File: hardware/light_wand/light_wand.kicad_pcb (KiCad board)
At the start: 2 copper layers, 21 parts, among them J1 1x1 Conn, J2 1x1 Conn, J3 1x1 Conn, J4 1x1 Conn, J5 1x1 Conn, J6 1x1 Conn, U1 TLV61070A, U4 Pico

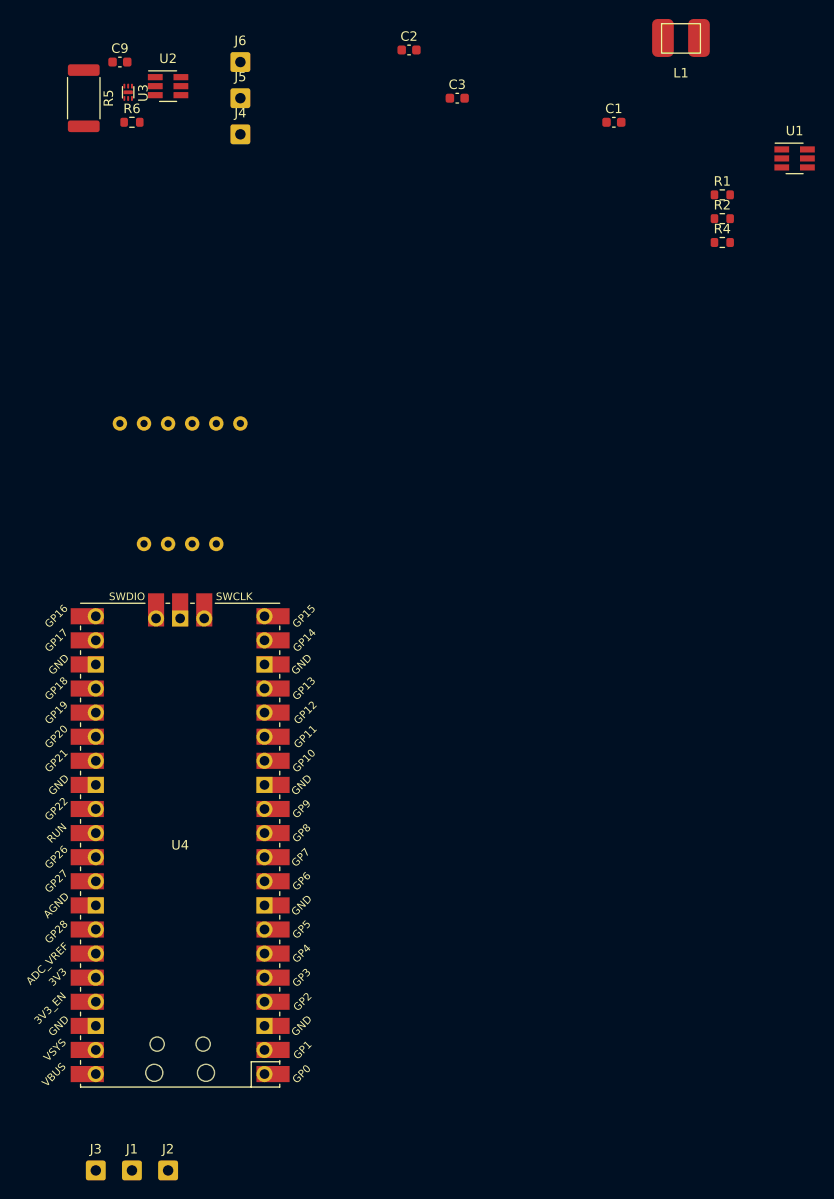
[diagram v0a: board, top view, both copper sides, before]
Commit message: Finished PCB layout
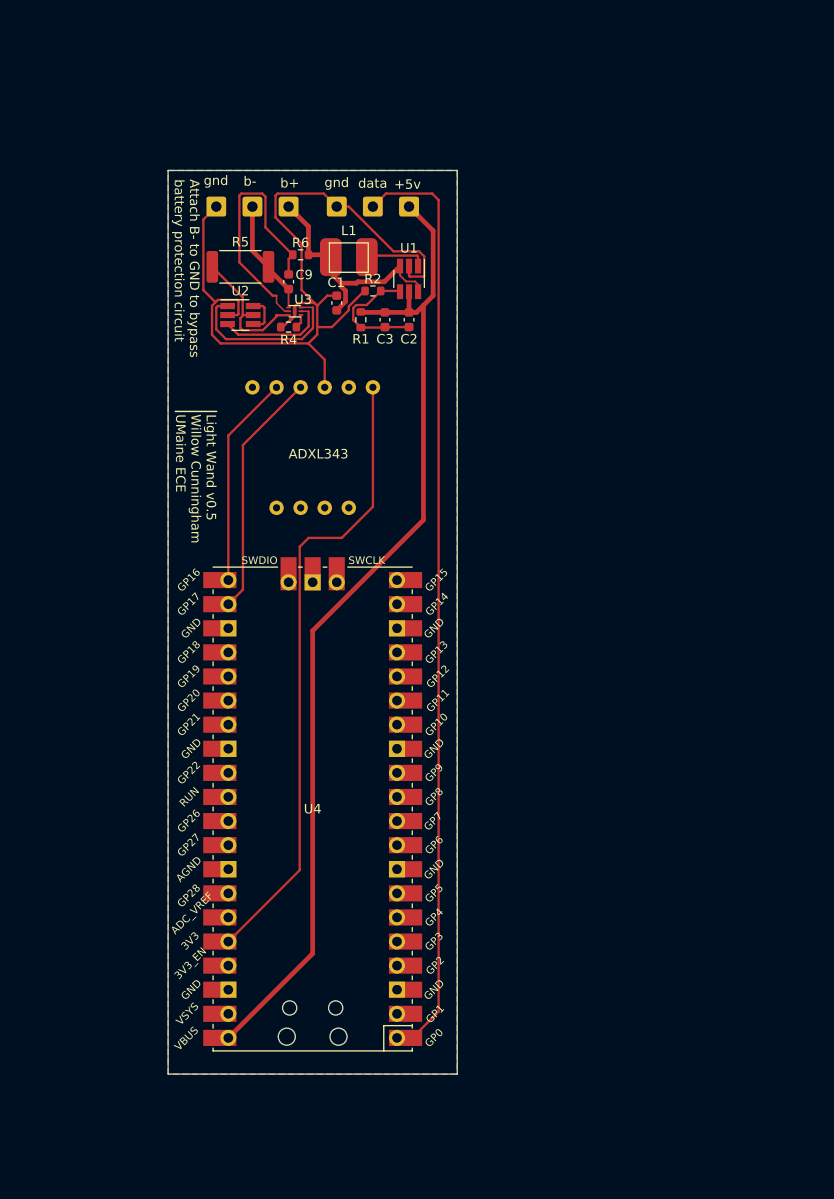
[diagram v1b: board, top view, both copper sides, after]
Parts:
- moved J1 104.7 mm to (146.1, 50.8)
- moved J2 104.7 mm to (149.9, 50.8)
- moved J3 104.7 mm to (142.2, 50.8)
- moved R4 46.6 mm to (137.2, 63.5)
- moved U1 42.6 mm to (149.9, 58.4), turned to -90 degrees
- moved L1 41.9 mm to (143.5, 60.3)
- moved R1 40.3 mm to (144.8, 62.7), turned to -90 degrees
- moved R2 37.6 mm to (146.1, 59.7), turned to 180 degrees
- moved C1 34.9 mm to (142.2, 61.0), turned to 90 degrees
- moved C9 29.2 mm to (137.2, 58.7), turned to -90 degrees
- moved U3 29.0 mm to (137.8, 61.8), turned to 180 degrees
- moved C2 28.4 mm to (149.9, 62.7), turned to -90 degrees
- moved U2 25.3 mm to (132.1, 62.2)
- moved C3 24.6 mm to (147.3, 62.7), turned to -90 degrees
- moved R5 24.3 mm to (132.1, 57.1), turned to 0 degrees
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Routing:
- net +5V: track 0.00 -> 106.7 mm
- net Net-(J1-Pin_1): track 0.00 -> 98.9 mm
- net GND: track 0.00 -> 91.4 mm
- net +3V3: track 0.00 -> 66.8 mm
- net Net-(U3-VDD): track 0.00 -> 27.4 mm
- net /Power Supply/Vin+: track 0.00 -> 26.0 mm
- net Net-(U4-GPIO17): track 0.00 -> 26.0 mm
- net Net-(U4-GPIO16): track 0.00 -> 22.4 mm
- net Net-(U2-G1): track 0.00 -> 18.1 mm
- net Net-(U2-S1): track 0.00 -> 14.9 mm
- net Net-(U1-FB): track 0.00 -> 13.2 mm
- net /Power Supply/Vin-: track 0.00 -> 12.2 mm
- net Net-(U2-G2): track 0.00 -> 11.8 mm
- net Net-(U1-SW): track 0.00 -> 6.53 mm
- net Net-(U2-D1): track 0.00 -> 4.09 mm
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- added copper zone on B.Cu, net GND
- added copper zone on F.Cu, net GND
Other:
- board outline added: 30.5 x 95.2 mm
- board text added: "+5v"
- board text added: "ADXL343"
- board text added: "Attach B- to GND to bypass battery protection circuit"
- board text added: "Light Wand v0.5 Willow Cunningham UMaine ECE"
- board text added: "b+"
- board text added: "b-"
- board text added: "data"
- board text added: "gnd"
